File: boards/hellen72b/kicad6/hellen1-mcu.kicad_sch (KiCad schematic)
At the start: 91 parts, among them J101 *

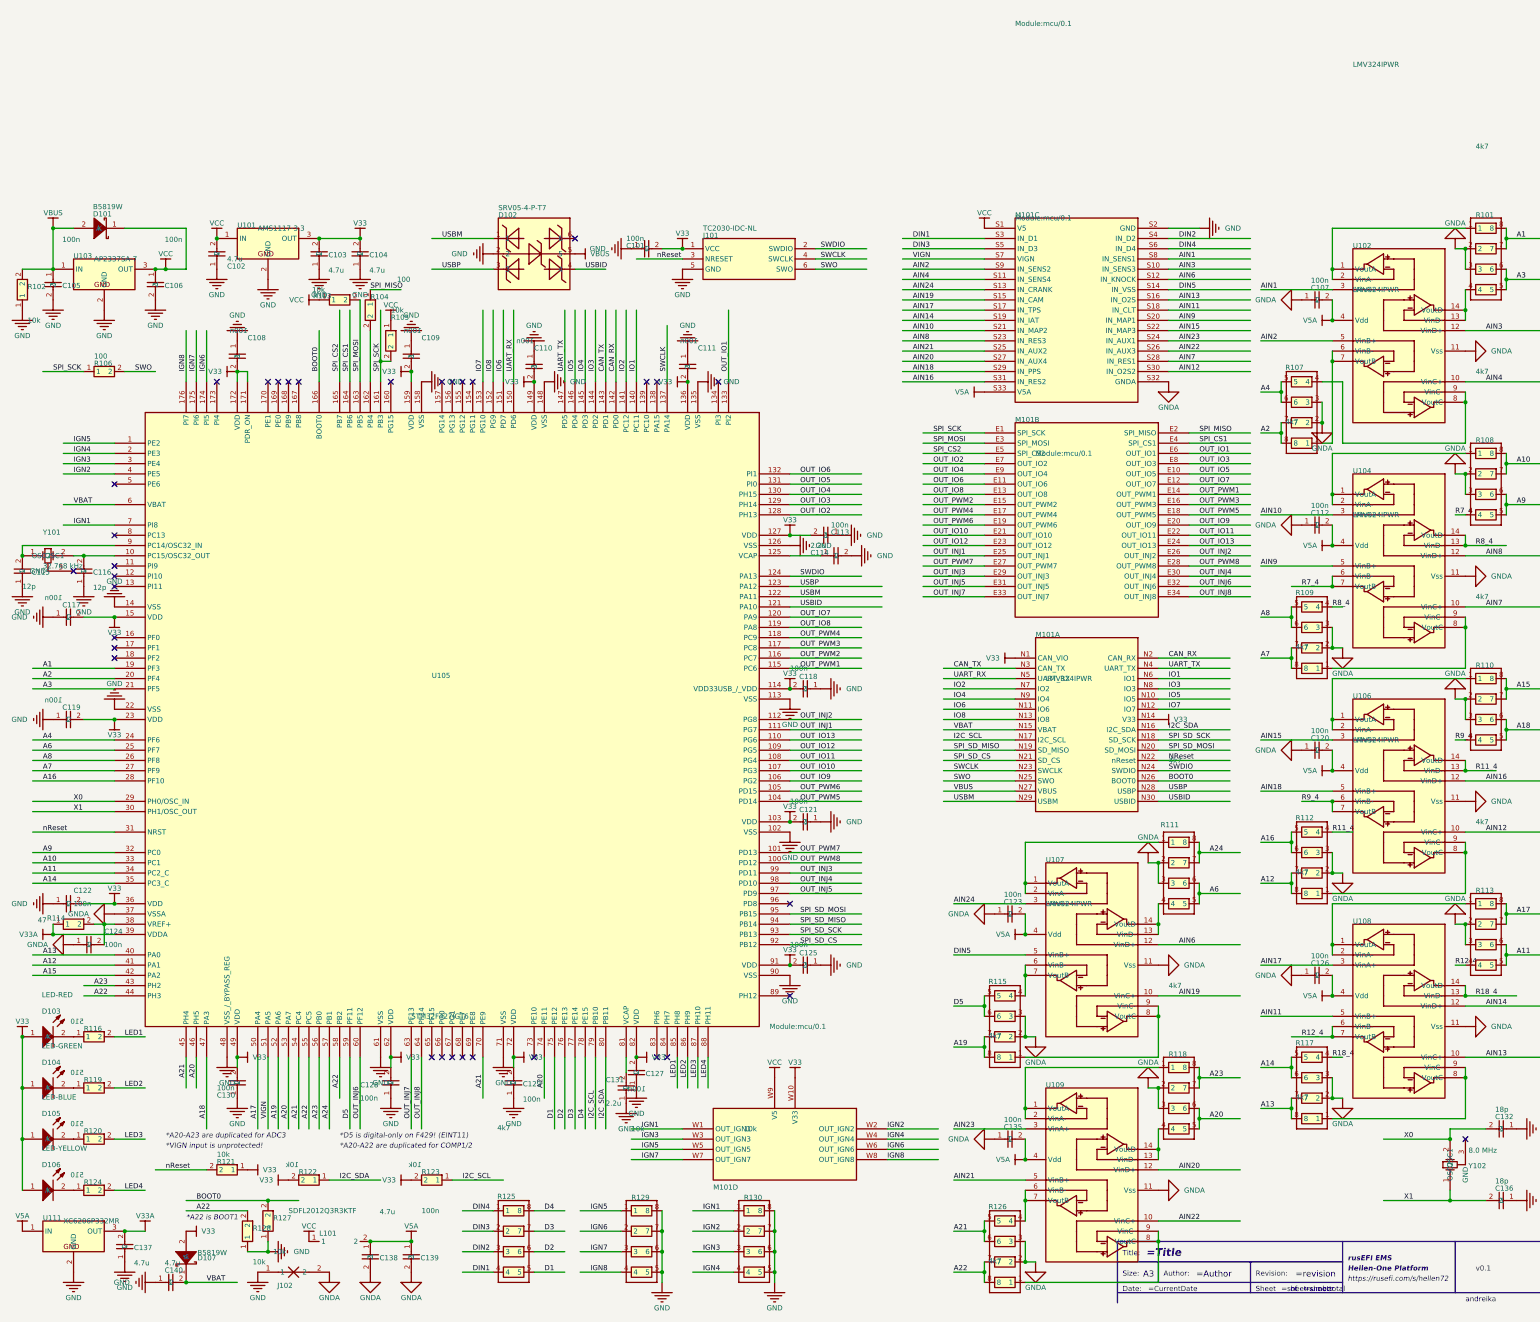
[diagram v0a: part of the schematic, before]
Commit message: update exported kicad files after refactoring
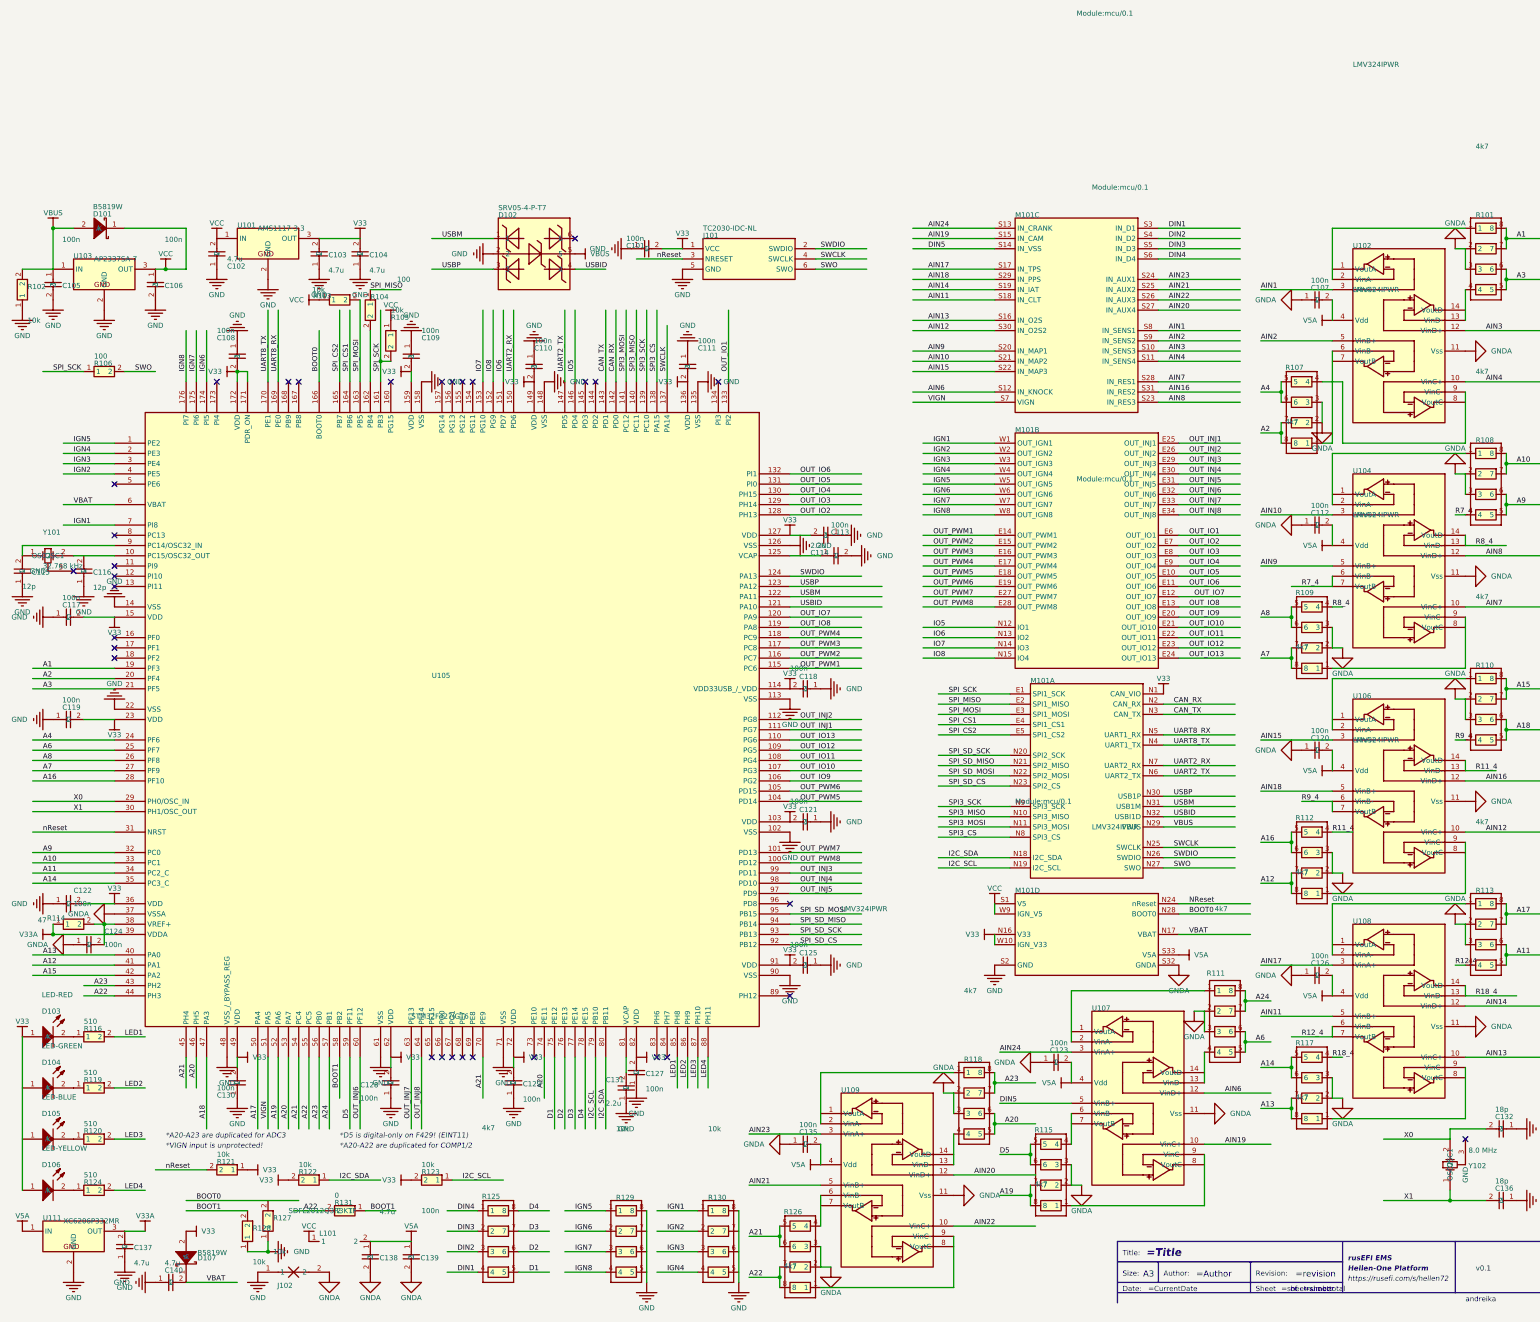
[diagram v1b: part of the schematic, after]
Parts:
- added R131: ~, symbol hellen1-mcu-altium-import:1_mirrored_Res
- C101, C102, C103, C104, C105, C106, C107, C108, C109, C110, C111, C112, C113, C114, C115, C116, C117, C118, C119, C120, C121, C122, C123, C124, C125, C126, C127, C128, C129, C130, C131, C132, C135, C136, C137, C138, C139, C140, D101, D102, D103, D104, D105, D106, D107, J102, M101, R102, R103, R104, R105, R106, R114, R116, R119, R120, R121, R122, R123, R124, R127, R128, R129, R130, U101, U102, U103, U104, U105, U106, U107, U108, U109, U111, Y101, Y102: value (none) -> ~
- R101, R107, R108, R109, R110, R111, R112, R113, R115, R117, R118, R125, R126: value (none) -> ~; Supplier Part Number 3 C1980 -> C66697
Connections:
- net A22: now also R131.2; no longer R128.2, U105.58 (PB2)
- net BOOT0: now also M101.N28 (BOOT0); no longer M101.N26 (BOOT0), R127.2
- net GND: now also M101.S2 (GND); no longer M101.S2 (GND), R129.5, R129.6, R129.7, R130.5, R130.6, R130.7
- net GNDA: now also M101.S32 (GNDA); no longer M101.S32 (GNDA)
- net I2C_SCL: now also M101.N19 (I2C_SCL); no longer M101.N17 (I2C_SCL)
- net I2C_SDA: now also M101.N18 (I2C_SDA); no longer M101.N16 (I2C_SDA)
- net IGN1: now also M101.W1 (OUT_IGN1); no longer M101.W1 (OUT_IGN1)
- net IGN2: now also M101.W2 (OUT_IGN2); no longer M101.W2 (OUT_IGN2)
- net IGN3: now also M101.W3 (OUT_IGN3); no longer M101.W3 (OUT_IGN3)
- net IGN4: now also M101.W4 (OUT_IGN4); no longer M101.W4 (OUT_IGN4)
- net IGN5: now also M101.W5 (OUT_IGN5); no longer M101.W5 (OUT_IGN5)
- net IGN6: now also M101.W6 (OUT_IGN6); no longer M101.W6 (OUT_IGN6)
- net IGN7: now also M101.W7 (OUT_IGN7); no longer M101.W7 (OUT_IGN7)
- net IGN8: now also M101.W8 (OUT_IGN8); no longer M101.W8 (OUT_IGN8)
- net IO5: now also M101.N12 (IO1); no longer M101.N10 (IO5)
- net IO6: now also M101.N13 (IO2); no longer M101.N11 (IO6)
- net IO7: now also M101.N14 (IO3); no longer M101.N12 (IO7)
- net IO8: now also M101.N15 (IO4); no longer M101.N13 (IO8)
- net NReset: now also M101.N24 (nReset); no longer M101.N22 (nReset)
- net SPI_CS1: now also M101.E4 (SPI1_CS1); no longer M101.E4 (SPI_CS1)
- net SPI_CS2: now also M101.E5 (SPI1_CS2); no longer M101.E5 (SPI_CS2)
- net SPI_MISO: now also M101.E2 (SPI1_MISO); no longer M101.E2 (SPI_MISO)
- net SPI_MOSI: now also M101.E3 (SPI1_MOSI); no longer M101.E3 (SPI_MOSI)
- net SPI_SCK: now also M101.E1 (SPI1_SCK); no longer M101.E1 (SPI_SCK)
- net SPI_SD_CS: now also M101.N23 (SPI2_CS); no longer M101.N21 (SD_CS)
- net SPI_SD_MISO: now also M101.N21 (SPI2_MISO); no longer M101.N19 (SD_MISO)
- net SPI_SD_MOSI: now also M101.N22 (SPI2_MOSI); no longer M101.N20 (SD_MOSI)
- net SPI_SD_SCK: now also M101.N20 (SPI2_SCK); no longer M101.N18 (SD_SCK)
- net SWCLK: now also M101.N25 (SWCLK); no longer M101.N23 (SWCLK)
- net SWDIO: now also M101.N26 (SWDIO); no longer M101.N24 (SWDIO)
- net SWO: now also M101.N27 (SWO); no longer M101.N25 (SWO)
- net USBID: now also M101.N32 (USBI1D); no longer M101.N30 (USBID)
- net USBM: now also M101.N31 (USB1M); no longer M101.N29 (USBM)
- net USBP: now also M101.N30 (USB1P); no longer M101.N28 (USBP)
- net V33: now also M101.N16 (V33); no longer D104.1 (A), D105.1 (A), M101.N14 (V33)
- net V5A: now also M101.S33 (V5A); no longer M101.S33 (V5A)
- net VBAT: now also M101.N17 (VBAT); no longer M101.N15 (VBAT)
- net VBUS: now also M101.N29 (VBUS); no longer M101.N27 (VBUS)
- net VCC: now also M101.S1 (V5); no longer M101.S1 (V5)
- net at R118.1, U109.2 (VinA-): no longer U109.1 (VoutA)
- net at R118.4, U109.13 (VinD-): no longer U109.14 (VoutD)
- net at R126.4, U109.6 (VinB-): no longer U109.7 (VoutB)
- net at R126.1, U109.9 (VinC-): no longer U109.8 (VoutC)
- net at U105.10 (PC15/OSC32_OUT), Y101.2 (OSC2): no longer C116.2
- net at R107.1, U102.6 (VinB-): no longer U102.7 (VoutB)
- net at R107.4, U102.9 (VinC-): no longer U102.8 (VoutC)
- net at R111.1, U107.2 (VinA-): no longer U107.1 (VoutA)
- net at R111.4, U107.13 (VinD-): no longer U107.14 (VoutD)
- net SPI3_CS: now reaches U105.138 (PA15)
- net SPI3_CS: now also M101.N8 (SPI3_CS)
- net SPI3_SCK: now reaches U105.139 (PC10)
- net SPI3_SCK: now also M101.N9 (SPI3_SCK)
- net UART8_RX: now reaches U105.169 (PE0)
- net UART8_RX: now also M101.N5 (UART1_RX)
- net UART8_TX: now reaches U105.170 (PE1)
- net UART8_TX: now also M101.N4 (UART1_TX)
- net at R108.1, U104.2 (VinA-): no longer U104.1 (VoutA)
- net at R110.1, U106.2 (VinA-): no longer U106.1 (VoutA)
- net at R112.1, U106.9 (VinC-): no longer U106.8 (VoutC)
- net at R113.1, U108.2 (VinA-): no longer U108.1 (VoutA)
- net at R117.1, U108.9 (VinC-): no longer U108.8 (VoutC)
- net at R101.1, U102.2 (VinA-): no longer U102.1 (VoutA)
- net at R101.4, U102.13 (VinD-): no longer U102.14 (VoutD)
- net at R109.1, U104.9 (VinC-): no longer U104.8 (VoutC)
- net at R115.1, U107.9 (VinC-): no longer U107.8 (VoutC)
- net at R115.4, U107.6 (VinB-): no longer U107.7 (VoutB)
- net IO1 renamed SPI3_MISO
- net SPI3_MISO: now also M101.N10 (SPI3_MISO); no longer M101.N6 (IO1)
- net IO2 renamed SPI3_MOSI
- net SPI3_MOSI: now also M101.N11 (SPI3_MOSI); no longer M101.N7 (IO2)
- net IO3: no longer names the net of U105.144 (PD2)
- net IO3: no longer M101.N8 (IO3)
- net IO4: no longer names the net of U105.145 (PD3)
- net IO4: no longer M101.N9 (IO4)
- net UART_RX renamed UART2_RX
- net UART2_RX: now also M101.N7 (UART2_RX); no longer M101.N5 (UART_RX)
- net UART_TX renamed UART2_TX
- net UART2_TX: now also M101.N6 (UART2_TX); no longer M101.N4 (UART_TX)
- new net BOOT1: R128.2, R131.1, U105.58 (PB2)
- no-connect marks 34 -> 32
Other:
- note removed: "*A22 is BOOT1"
